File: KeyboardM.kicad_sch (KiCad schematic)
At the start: 12 parts, among them U1 ATmega32U4-A

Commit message: ISP Header
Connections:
- net +5V: now also J?.2 (VCC)
- net GND: now also J?.6 (GND)
- net RESET: now also J?.5 (~{RST})
- net MISO: now reaches J?.1 (MISO)
- net MISO: now also U1.11 (PB3)
- net SCK: now reaches J?.3 (SCK)
- net SCK: now also U1.9 (PB1)
- net MOSI: now reaches J?.4 (MOSI)
- net MOSI: now also U1.10 (PB2)
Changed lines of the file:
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@@
     (stroke (width 0) (type default) (color 0 0 0 0))
+  )
+  (global_label "RESET" (shape input) (at 63.5 78.74 0) (fields_autoplaced)
+    (effects (font (size 1.27 1.27)) (justify left))
+    (property "Intersheet References" "${INTERSHEET_REFS}" (id 0) (at 71.6583 78.6606 0)
+      (effects (font (size 1.27 1.27)) (justify left) hide)
+    )
   )
   (global_label "XTAL2" (shape input) (at 102.87 69.85 90) (fields_autoplaced)
@@
     )
   )
+  (global_label "MISO" (shape input) (at 63.5 71.12 0) (fields_autoplaced)
+    (effects (font (size 1.27 1.27)) (justify left))
+    (property "Intersheet References" "${INTERSHEET_REFS}" (id 0) (at 70.5093 71.0406 0)
+      (effects (font (size 1.27 1.27)) (justify left) hide)
+    )
+  )
   (global_label "XTAL1" (shape input) (at 128.27 72.39 180) (fields_autoplaced)
     (effects (font (size 1.27 1.27)) (justify right))
@@
     )
   )
+  (global_label "SCK" (shape input) (at 63.5 76.2 0) (fields_autoplaced)
+    (effects (font (size 1.27 1.27)) (justify left))
+    (property "Intersheet References" "${INTERSHEET_REFS}" (id 0) (at 69.6626 76.1206 0)
+      (effects (font (size 1.27 1.27)) (justify left) hide)
+    )
+  )
+  (global_label "MOSI" (shape input) (at 63.5 73.66 0) (fields_autoplaced)
+    (effects (font (size 1.27 1.27)) (justify left))
+    (property "Intersheet References" "${INTERSHEET_REFS}" (id 0) (at 70.5093 73.5806 0)
+      (effects (font (size 1.27 1.27)) (justify left) hide)
+    )
+  )
   (global_label "XTAL2" (shape input) (at 128.27 77.47 180) (fields_autoplaced)
     (effects (font (size 1.27 1.27)) (justify right))
@@
     )
   )
+  (global_label "MISO" (shape input) (at 158.75 74.93 0) (fields_autoplaced)
+    (effects (font (size 1.27 1.27)) (justify left))
+    (property "Intersheet References" "${INTERSHEET_REFS}" (id 0) (at 165.7593 74.8506 0)
+      (effects (font (size 1.27 1.27)) (justify left) hide)
+    )
+  )
+  (global_label "SCK" (shape input) (at 158.75 69.85 0) (fields_autoplaced)
+    (effects (font (size 1.27 1.27)) (justify left))
+    (property "Intersheet References" "${INTERSHEET_REFS}" (id 0) (at 164.9126 69.7706 0)
+      (effects (font (size 1.27 1.27)) (justify left) hide)
+    )
+  )
+  (global_label "MOSI" (shape input) (at 158.75 72.39 0) (fields_autoplaced)
+    (effects (font (size 1.27 1.27)) (justify left))
+    (property "Intersheet References" "${INTERSHEET_REFS}" (id 0) (at 165.7593 72.3106 0)
+      (effects (font (size 1.27 1.27)) (justify left) hide)
+    )
+  )
   (global_label "XTAL1" (shape input) (at 87.63 69.85 90) (fields_autoplaced)
     (effects (font (size 1.27 1.27)) (justify left))
@@
     (pin "5")
     (pin "6")
+  )
+  (symbol (lib_id "power:GND") (at 50.8 86.36 0) (unit 1)
+    (in_bom yes) (on_board yes) (fields_autoplaced)
+    (property "Reference" "#PWR?" (id 0) (at 50.8 92.71 0)
+      (effects (font (size 1.27 1.27)) hide)
+    )
+    (property "Value" "GND" (id 1) (at 50.8 91.44 0))
+    (property "Footprint" "" (id 2) (at 50.8 86.36 0)
+      (effects (font (size 1.27 1.27)) hide)
+    )
+    (property "Datasheet" "" (id 3) (at 50.8 86.36 0)
+      (effects (font (size 1.27 1.27)) hide)
+    )
+    (pin "1")
   )
   (symbol (lib_id "Device:C_Small") (at 100.33 130.81 0) (unit 1)
@@
     (pin "9")
   )
+  (symbol (lib_id "power:+5V") (at 50.8 63.5 0) (unit 1)
+    (in_bom yes) (on_board yes) (fields_autoplaced)
+    (property "Reference" "#PWR?" (id 0) (at 50.8 67.31 0)
+      (effects (font (size 1.27 1.27)) hide)
+    )
+    (property "Value" "+5V" (id 1) (at 50.8 58.42 0))
+    (property "Footprint" "" (id 2) (at 50.8 63.5 0)
+      (effects (font (size 1.27 1.27)) hide)
+    )
+    (property "Datasheet" "" (id 3) (at 50.8 63.5 0)
+      (effects (font (size 1.27 1.27)) hide)
+    )
+    (pin "1")
+  )
   (symbol (lib_id "Device:C_Small") (at 102.87 78.74 0) (unit 1)
     (in_bom yes) (on_board yes) (fields_autoplaced)
@@
       (reference "#PWR?") (unit 1) (value "GND") (footprint "")
     )
+    (path "/3bd5d607-5d90-461d-9e03-623ce54f8a63"
+      (reference "#PWR?") (unit 1) (value "GND") (footprint "")
+    )
     (path "/4dbb1b14-93b7-481b-9fc7-7ec555f93957"
       (reference "#PWR?") (unit 1) (value "+5V") (footprint "")
@@
       (reference "#PWR?") (unit 1) (value "GND") (footprint "")
     )
+    (path "/bde56c9e-c398-4c7d-a88d-532a00b6e85f"
+      (reference "#PWR?") (unit 1) (value "+5V") (footprint "")
+    )
     (path "/29a715ce-be66-4c11-bd1a-2950b0c010d7"

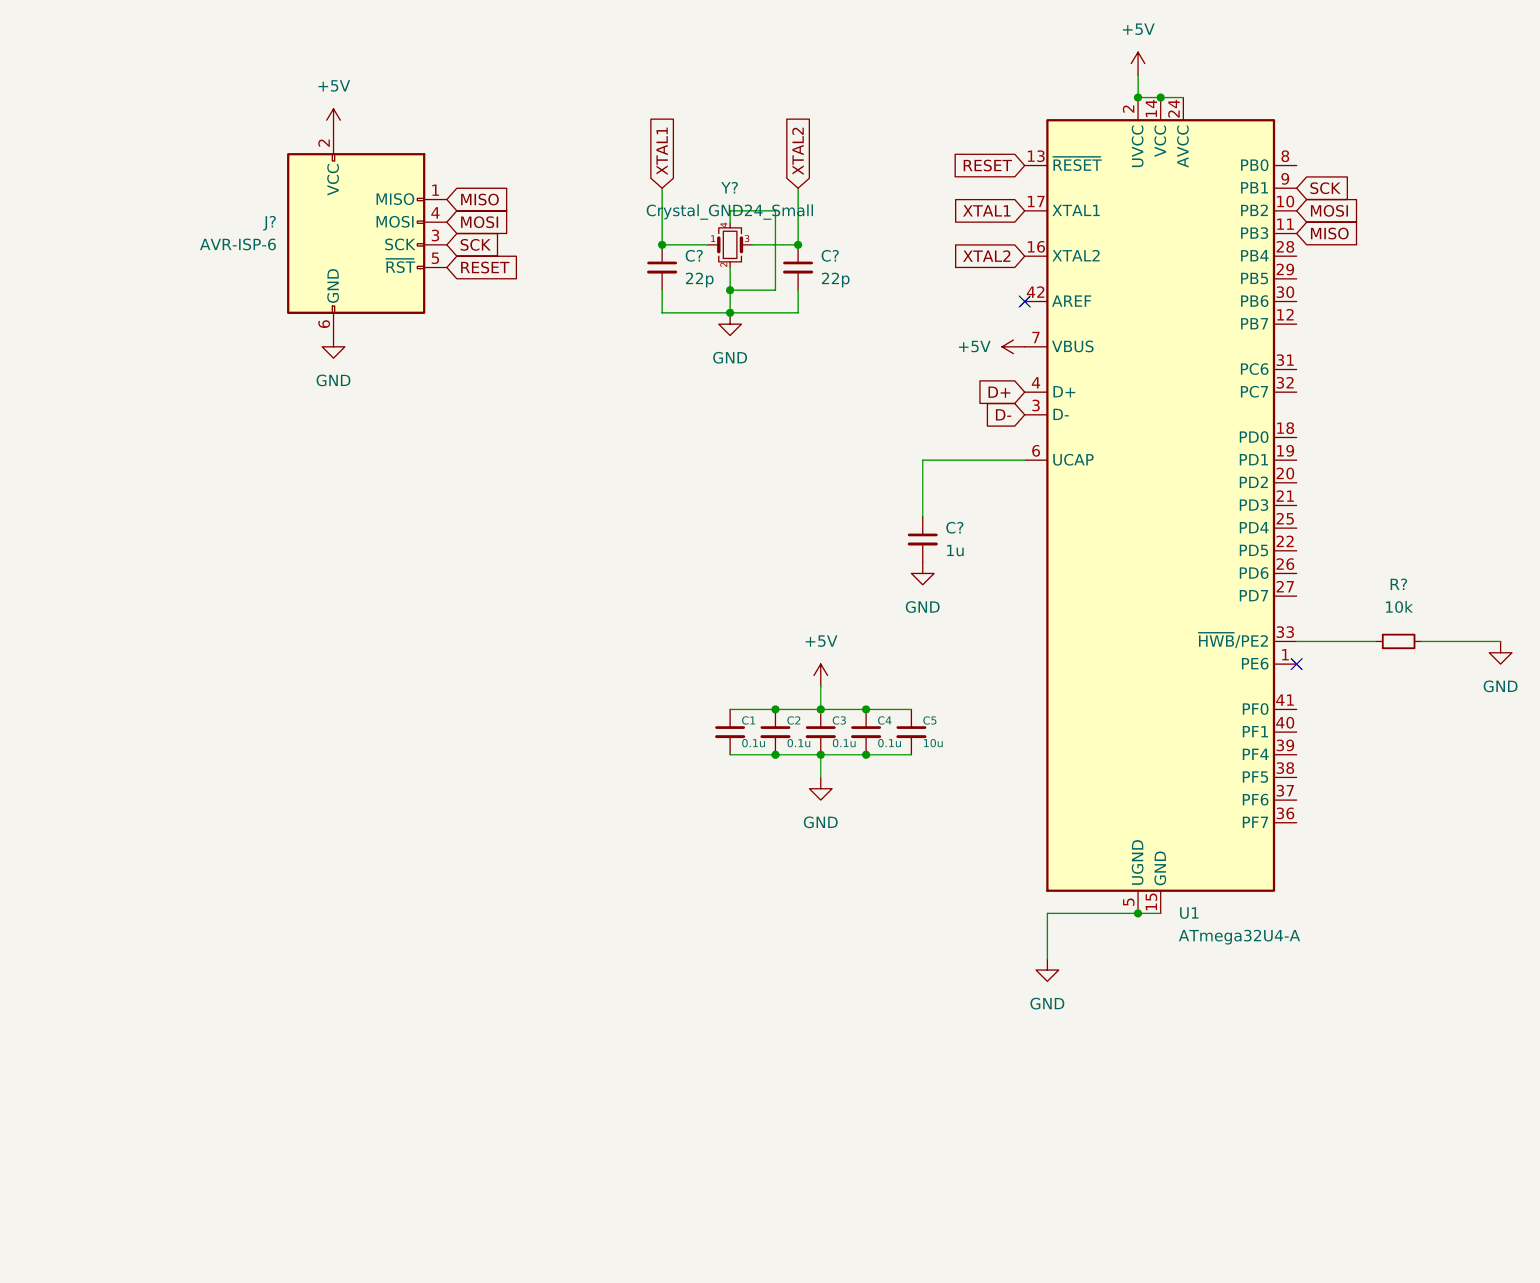
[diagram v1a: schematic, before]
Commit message: MX Only Footprint Library
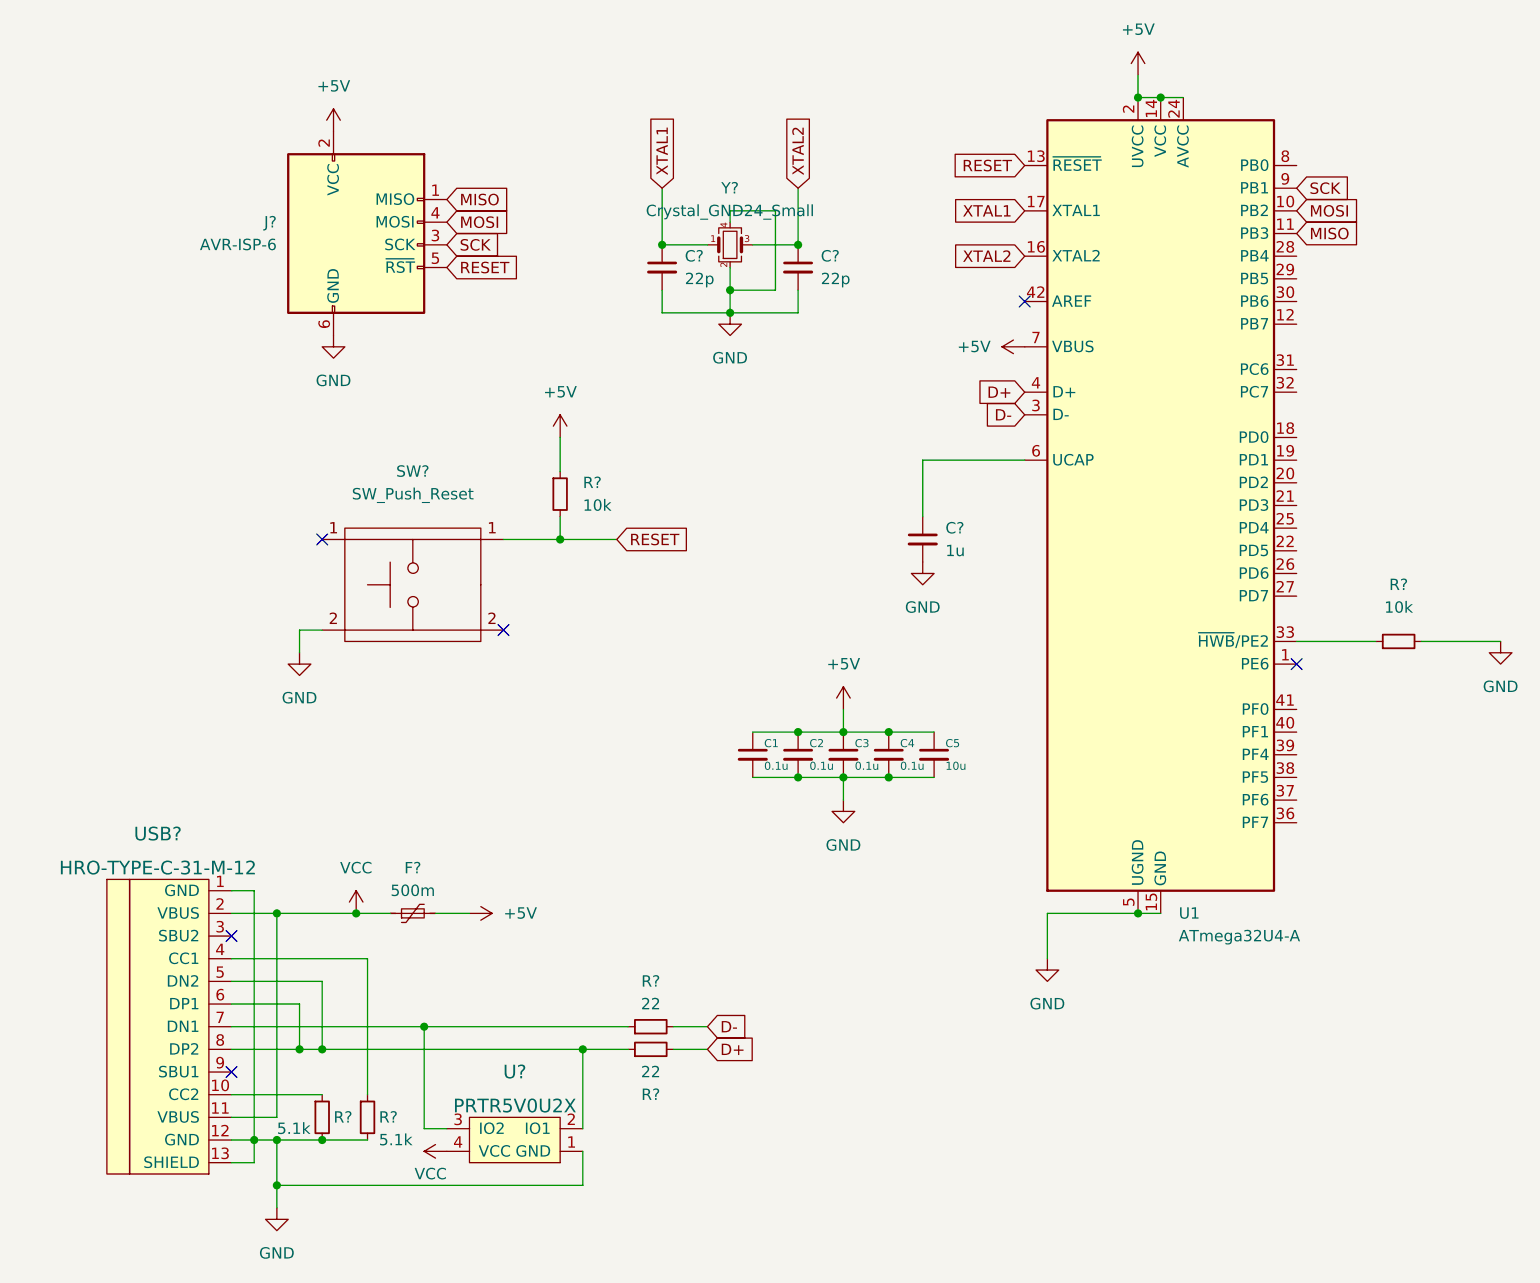
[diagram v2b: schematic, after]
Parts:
- added F?: 500m, symbol Device:Polyfuse_Small
- added R? (x2): 22, symbol Device:R_Small
- added R?: 10k, symbol Device:R_Small
- added R? (x2): 5.1k, symbol Device:R_Small
- added SW?: SW_Push_Reset, symbol SW_SK:SW_SKQG
- added U?: PRTR5V0U2X, symbol random-keyboard-parts:PRTR5V0U2X
- added USB?: HRO-TYPE-C-31-M-12, symbol Type-C:HRO-TYPE-C-31-M-12
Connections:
- net +5V: now also F?.2, R?.1
- net D+: now also R?.2
- net D-: now also R?.2
- net GND: now also R?.2, R?.2, SW?., U?.1 (GND), USB?.1 (GND), USB?.12 (GND), USB?.13 (SHIELD)
- net RESET: now also R?.2, SW?.
- new net: R?.1, U?.2 (IO1), USB?.5 (DN2), USB?.6 (DP1), USB?.8 (DP2)
- new net: R?.1, U?.3 (IO2), USB?.7 (DN1)
- new net: R?.1, USB?.10 (CC2)
- new net: R?.1, USB?.4 (CC1)
- new net VCC: F?.1, U?.4 (VCC), USB?.11 (VBUS), USB?.2 (VBUS)
- no-connect marks 2 -> 6
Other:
- moved on the sheet: C1, C2, C3, C4, C5
